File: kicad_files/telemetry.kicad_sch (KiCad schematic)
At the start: 24 parts, among them J6 RFD900ux 10 Pin Header, J7 Conn_ARM_JTAG_SWD_10, J8 RFD900ux 3 Pin Power Select, J9 USB_C_Receptacle_USB2.0_16P, U8 74LVC1G125, U9 WE-TVS-82400102

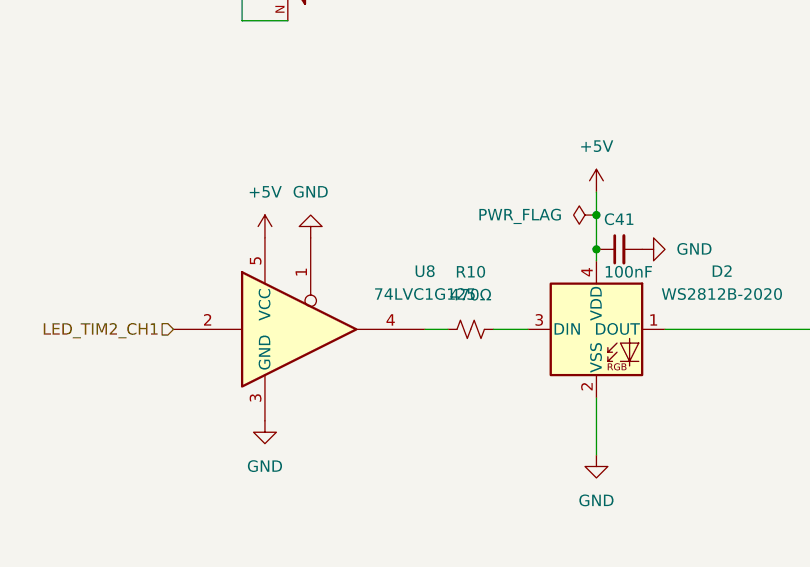
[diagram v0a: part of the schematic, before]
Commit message: add 3d models
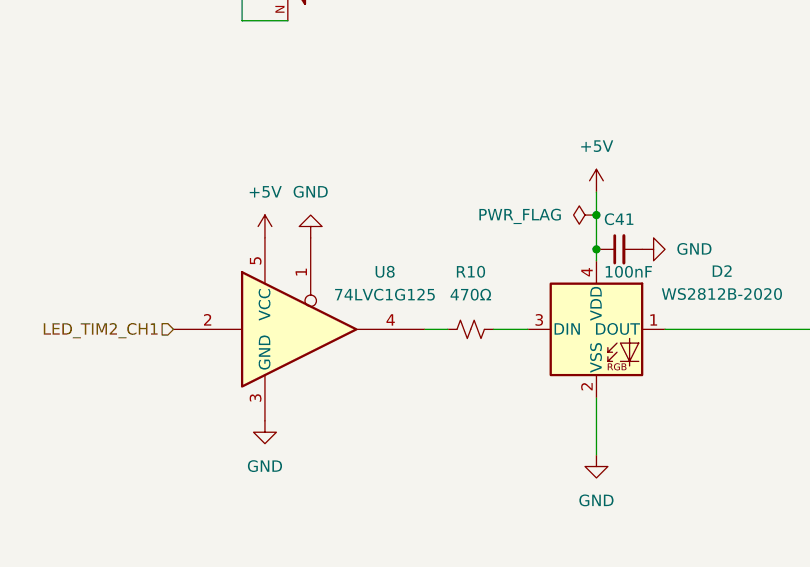
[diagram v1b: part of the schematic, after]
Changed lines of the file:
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@@
 		(in_pos_files yes)
 		(dnp no)
-		(fields_autoplaced yes)
 		(property "Reference" "U8"
-			(at 60.96 79.9398 0)
+			(at 56.515 80.01 0)
 			(show_name no)
 			(do_not_autoplace no)
@@
 		)
 		(property "Value" "74LVC1G125"
-			(at 60.96 82.4798 0)
+			(at 56.515 82.55 0)
 			(show_name no)
 			(do_not_autoplace no)

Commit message: fix pyro adc
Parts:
- renumbered C41 to C39, C42 to C40, C43 to C41, C44 to C42, C45 to C43, C46 to C44, C47 to C45, J6 to J5, J7 to J6, J8 to J7, J9 to J8
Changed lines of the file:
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@@
 		(dnp no)
 		(fields_autoplaced yes)
-		(property "Reference" "J6"
+		(property "Reference" "J5"
 			(at 106.68 120.65 0)
 			(show_name no)
@@
 			(project "versorlite"
 				(path "/1a230af0-0a74-48f7-8607-b087121dda49/4d884b5c-b332-4347-90a4-1c2e65497882"
-					(reference "J6")
+					(reference "J5")
 					(unit 1)
 				)
@@
 		(in_pos_files yes)
 		(dnp no)
-		(property "Reference" "C41"
+		(property "Reference" "C39"
 			(at 82.5563 74.168 90)
 			(show_name no)
@@
 			(project "versorlite"
 				(path "/1a230af0-0a74-48f7-8607-b087121dda49/4d884b5c-b332-4347-90a4-1c2e65497882"
-					(reference "C41")
+					(reference "C39")
 					(unit 1)
 				)
@@
 		(dnp no)
 		(fields_autoplaced yes)
-		(property "Reference" "C46"
+		(property "Reference" "C44"
 			(at 248.9263 38.1 90)
 			(show_name no)
@@
 			(project "versorlite"
 				(path "/1a230af0-0a74-48f7-8607-b087121dda49/4d884b5c-b332-4347-90a4-1c2e65497882"
-					(reference "C46")
+					(reference "C44")
 					(unit 1)
 				)
@@
 		(dnp no)
 		(fields_autoplaced yes)
-		(property "Reference" "C47"
+		(property "Reference" "C45"
 			(at 248.9263 45.72 90)
 			(show_name no)
@@
 			(project "versorlite"
 				(path "/1a230af0-0a74-48f7-8607-b087121dda49/4d884b5c-b332-4347-90a4-1c2e65497882"
-					(reference "C47")
+					(reference "C45")
 					(unit 1)
 				)
@@
 		(dnp no)
 		(fields_autoplaced yes)
-		(property "Reference" "J8"
+		(property "Reference" "J7"
 			(at 146.05 119.38 0)
 			(show_name no)
@@
 			(project "versorlite"
 				(path "/1a230af0-0a74-48f7-8607-b087121dda49/4d884b5c-b332-4347-90a4-1c2e65497882"
-					(reference "J8")
+					(reference "J7")
 					(unit 1)
 				)
@@
 		(dnp no)
 		(fields_autoplaced yes)
-		(property "Reference" "J9"
+		(property "Reference" "J8"
 			(at 201.93 59.69 0)
 			(show_name no)
@@
 			(project "versorlite"
 				(path "/1a230af0-0a74-48f7-8607-b087121dda49/4d884b5c-b332-4347-90a4-1c2e65497882"
-					(reference "J9")
+					(reference "J8")
 					(unit 1)
 				)
@@
 		(in_pos_files yes)
 		(dnp no)
-		(property "Reference" "C44"
+		(property "Reference" "C42"
 			(at 152.4 157.4863 90)
 			(show_name no)
@@
 			(project "versorlite"
 				(path "/1a230af0-0a74-48f7-8607-b087121dda49/4d884b5c-b332-4347-90a4-1c2e65497882"
-					(reference "C44")
+					(reference "C42")
 					(unit 1)
 				)
@@
 		(in_pos_files yes)
 		(dnp no)
-		(property "Reference" "C42"
+		(property "Reference" "C40"
 			(at 115.5763 72.898 90)
 			(show_name no)
@@
 			(project "versorlite"
 				(path "/1a230af0-0a74-48f7-8607-b087121dda49/4d884b5c-b332-4347-90a4-1c2e65497882"
-					(reference "C42")
+					(reference "C40")
 					(unit 1)
 				)
@@
 		(dnp no)
 		(fields_autoplaced yes)
-		(property "Reference" "C45"
+		(property "Reference" "C43"
 			(at 162.56 155.5749 0)
 			(show_name no)
@@
 			(project "versorlite"
 				(path "/1a230af0-0a74-48f7-8607-b087121dda49/4d884b5c-b332-4347-90a4-1c2e65497882"
-					(reference "C45")
+					(reference "C43")
 					(unit 1)
 				)
@@
 		(in_pos_files yes)
 		(dnp no)
-		(property "Reference" "C43"
+		(property "Reference" "C41"
 			(at 143.002 157.4863 90)
 			(show_name no)
@@
 			(project "versorlite"
 				(path "/1a230af0-0a74-48f7-8607-b087121dda49/4d884b5c-b332-4347-90a4-1c2e65497882"
-					(reference "C43")
+					(reference "C41")
 					(unit 1)
 				)
@@
 		(dnp no)
 		(fields_autoplaced yes)
-		(property "Reference" "J7"
+		(property "Reference" "J6"
 			(at 133.35 53.3399 0)
 			(show_name no)
@@
 			(project "versorlite"
 				(path "/1a230af0-0a74-48f7-8607-b087121dda49/4d884b5c-b332-4347-90a4-1c2e65497882"
-					(reference "J7")
+					(reference "J6")
 					(unit 1)
 				)

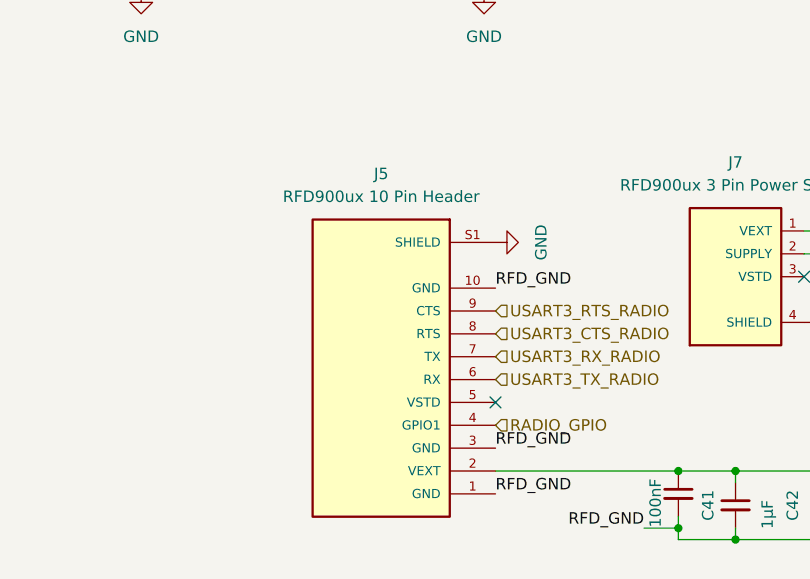
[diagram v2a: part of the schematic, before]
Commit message: more jlcpcb, change jst gh header
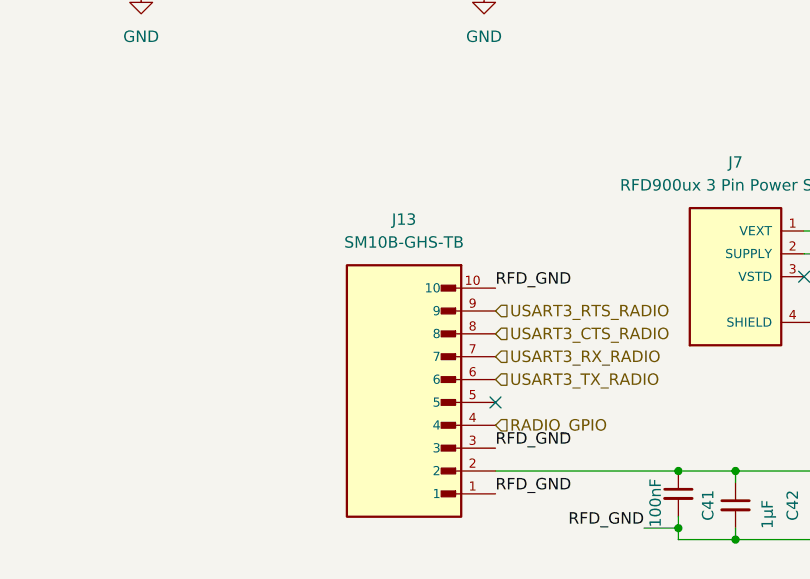
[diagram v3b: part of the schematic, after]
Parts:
- removed J5: RFD900ux 10 Pin Header, footprints:JST_BM10B-GHS-TBT_LF__SN__N_, symbol BM10B-GHS-TBT_LF__SN__N_:BM10B-GHS-TBT_LF__SN__N_
- added J13: SM10B-GHS-TB, footprints:JST_SM10B-GHS-TB, symbol SM10B-GHS-TB:SM10B-GHS-TB
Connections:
- net +5V: now also J13.2
- net GND: now also J13.1, J13.10, J13.3
- net RADIO_GPIO: now also J13.4
- net USART3_CTS_RADIO: now also J13.8
- net USART3_RTS_RADIO: now also J13.9
- net USART3_RX_RADIO: now also J13.7
- net USART3_TX_RADIO: now also J13.6

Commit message: jlcstuffs
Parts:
- D4: footprint Diode_SMD:D_SOD-323F -> Diode_SMD:D_SOD-882
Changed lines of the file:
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@@
 			)
 		)
-		(property "Footprint" "Diode_SMD:D_SOD-323F"
+		(property "Footprint" "Diode_SMD:D_SOD-882"
 			(at 223.52 60.96 0)
 			(hide yes)

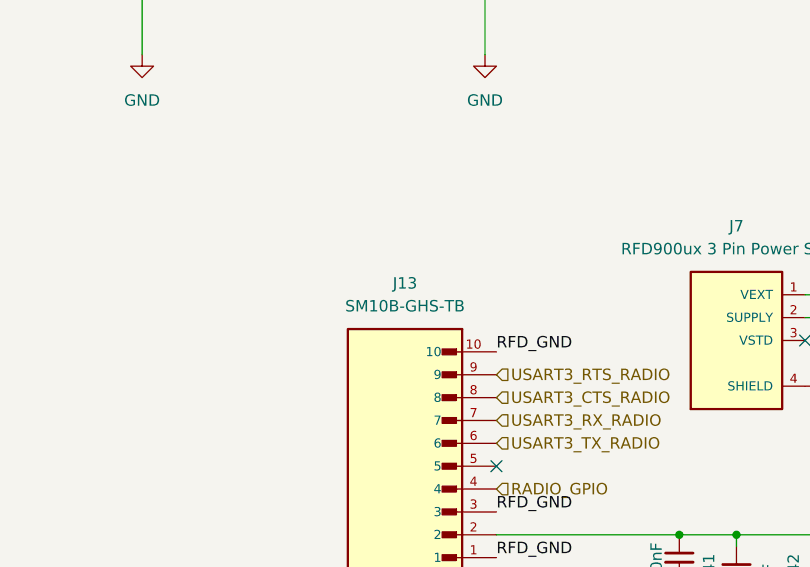
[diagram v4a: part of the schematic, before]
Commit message: fix schem for buck conv
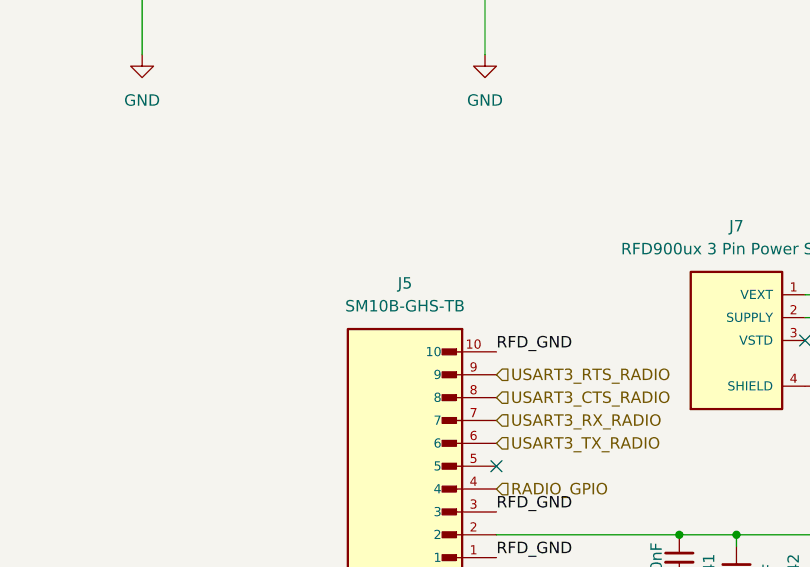
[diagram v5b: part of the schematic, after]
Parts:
- renumbered J13 to J5
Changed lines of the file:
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@@
 		(dnp no)
 		(fields_autoplaced yes)
-		(property "Reference" "#PWR063"
+		(property "Reference" "#PWR062"
 			(at 160.02 137.16 0)
 			(hide yes)
@@
 			(project "versorlite"
 				(path "/1a230af0-0a74-48f7-8607-b087121dda49/4d884b5c-b332-4347-90a4-1c2e65497882"
-					(reference "#PWR063")
+					(reference "#PWR062")
 					(unit 1)
 				)
@@
 		(dnp no)
 		(fields_autoplaced yes)
-		(property "Reference" "#PWR064"
+		(property "Reference" "#PWR063"
 			(at 171.45 161.29 0)
 			(hide yes)
@@
 			(project "versorlite"
 				(path "/1a230af0-0a74-48f7-8607-b087121dda49/4d884b5c-b332-4347-90a4-1c2e65497882"
-					(reference "#PWR064")
+					(reference "#PWR063")
 					(unit 1)
 				)
@@
 		(dnp no)
 		(fields_autoplaced yes)
-		(property "Reference" "#PWR070"
+		(property "Reference" "#PWR069"
 			(at 224.79 85.09 0)
 			(hide yes)
@@
 			(project "versorlite"
 				(path "/1a230af0-0a74-48f7-8607-b087121dda49/4d884b5c-b332-4347-90a4-1c2e65497882"
-					(reference "#PWR070")
+					(reference "#PWR069")
 					(unit 1)
 				)
@@
 		(dnp no)
 		(fields_autoplaced yes)
-		(property "Reference" "#PWR060"
+		(property "Reference" "#PWR059"
 			(at 142.24 76.2 0)
 			(hide yes)
@@
 			(project "versorlite"
 				(path "/1a230af0-0a74-48f7-8607-b087121dda49/4d884b5c-b332-4347-90a4-1c2e65497882"
-					(reference "#PWR060")
+					(reference "#PWR059")
 					(unit 1)
 				)
@@
 		(dnp no)
 		(fields_autoplaced yes)
-		(property "Reference" "#PWR069"
+		(property "Reference" "#PWR068"
 			(at 237.49 74.93 0)
 			(hide yes)
@@
 			(project "versorlite"
 				(path "/1a230af0-0a74-48f7-8607-b087121dda49/4d884b5c-b332-4347-90a4-1c2e65497882"
-					(reference "#PWR069")
+					(reference "#PWR068")
 					(unit 1)
 				)
@@
 		(in_pos_files yes)
 		(dnp no)
-		(property "Reference" "#PWR066"
+		(property "Reference" "#PWR065"
 			(at 201.93 125.73 0)
 			(hide yes)
@@
 			(project "versorlite"
 				(path "/1a230af0-0a74-48f7-8607-b087121dda49/4d884b5c-b332-4347-90a4-1c2e65497882"
-					(reference "#PWR066")
+					(reference "#PWR065")
 					(unit 1)
 				)
@@
 		(dnp no)
 		(fields_autoplaced yes)
-		(property "Reference" "#PWR065"
+		(property "Reference" "#PWR064"
 			(at 162.56 153.67 0)
 			(hide yes)
@@
 			(project "versorlite"
 				(path "/1a230af0-0a74-48f7-8607-b087121dda49/4d884b5c-b332-4347-90a4-1c2e65497882"
-					(reference "#PWR065")
+					(reference "#PWR064")
 					(unit 1)
 				)
@@
 		(dnp no)
 		(fields_autoplaced yes)
-		(property "Reference" "#PWR068"
+		(property "Reference" "#PWR067"
 			(at 237.49 72.39 0)
 			(hide yes)
@@
 			(project "versorlite"
 				(path "/1a230af0-0a74-48f7-8607-b087121dda49/4d884b5c-b332-4347-90a4-1c2e65497882"
-					(reference "#PWR068")
+					(reference "#PWR067")
 					(unit 1)
 				)
@@
 		(in_pos_files yes)
 		(dnp no)
-		(property "Reference" "#PWR061"
+		(property "Reference" "#PWR060"
 			(at 144.78 43.18 0)
 			(hide yes)
@@
 			(project "versorlite"
 				(path "/1a230af0-0a74-48f7-8607-b087121dda49/4d884b5c-b332-4347-90a4-1c2e65497882"
-					(reference "#PWR061")
+					(reference "#PWR060")
 					(unit 1)
 				)
@@
 		(dnp no)
 		(fields_autoplaced yes)
-		(property "Reference" "#PWR067"
+		(property "Reference" "#PWR066"
 			(at 223.52 46.99 0)
 			(hide yes)
@@
 			(project "versorlite"
 				(path "/1a230af0-0a74-48f7-8607-b087121dda49/4d884b5c-b332-4347-90a4-1c2e65497882"
-					(reference "#PWR067")
+					(reference "#PWR066")
 					(unit 1)
 				)
@@
 		(dnp no)
 		(fields_autoplaced yes)
-		(property "Reference" "J13"
+		(property "Reference" "J5"
 			(at 109.22 125.73 0)
 			(show_name no)
@@
 			(project "versorlite"
 				(path "/1a230af0-0a74-48f7-8607-b087121dda49/4d884b5c-b332-4347-90a4-1c2e65497882"
-					(reference "J13")
+					(reference "J5")
 					(unit 1)
 				)
@@
 		(dnp no)
 		(fields_autoplaced yes)
-		(property "Reference" "#PWR062"
+		(property "Reference" "#PWR061"
 			(at 144.78 76.2 0)
 			(hide yes)
@@
 			(project "versorlite"
 				(path "/1a230af0-0a74-48f7-8607-b087121dda49/4d884b5c-b332-4347-90a4-1c2e65497882"
-					(reference "#PWR062")
+					(reference "#PWR061")
 					(unit 1)
 				)
@@
 		(dnp no)
 		(fields_autoplaced yes)
-		(property "Reference" "#PWR071"
+		(property "Reference" "#PWR070"
 			(at 262.89 48.26 0)
 			(hide yes)
@@
 			(project "versorlite"
 				(path "/1a230af0-0a74-48f7-8607-b087121dda49/4d884b5c-b332-4347-90a4-1c2e65497882"
-					(reference "#PWR071")
-					(unit 1)
-				)
+					(reference "#PWR070")
+					(unit 1)
+				)
